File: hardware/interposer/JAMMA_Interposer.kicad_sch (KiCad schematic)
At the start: 5 parts

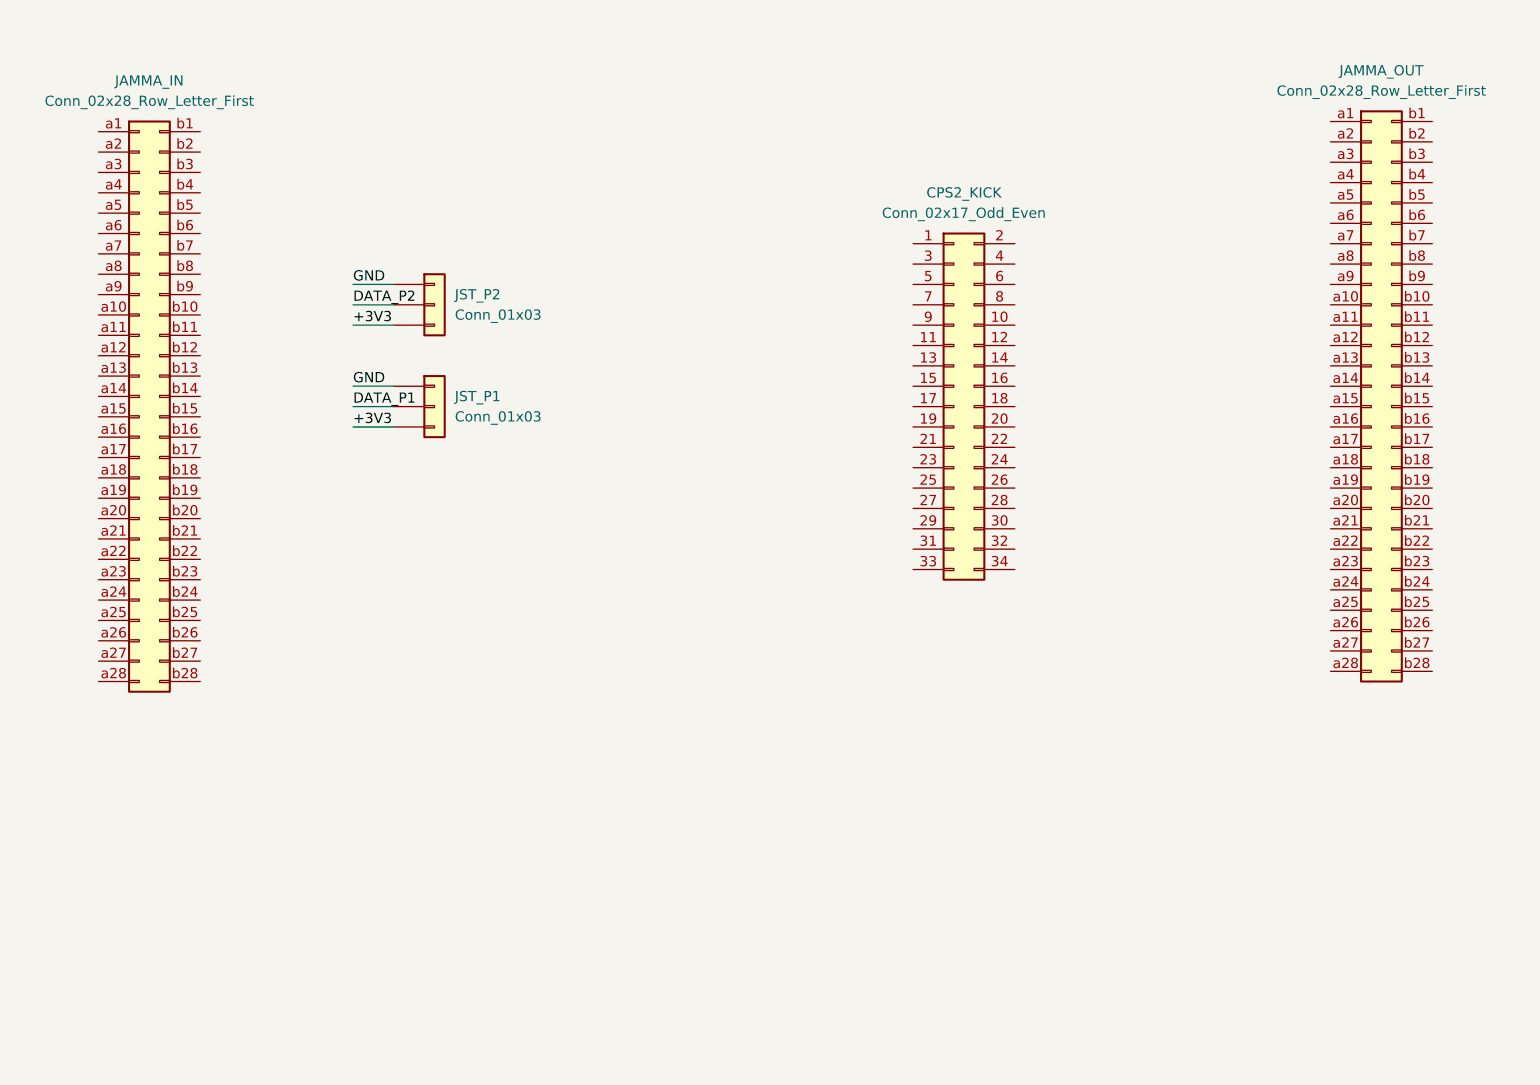
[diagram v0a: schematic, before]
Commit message: Update pin mapping/web assets and interposer schematic baseline
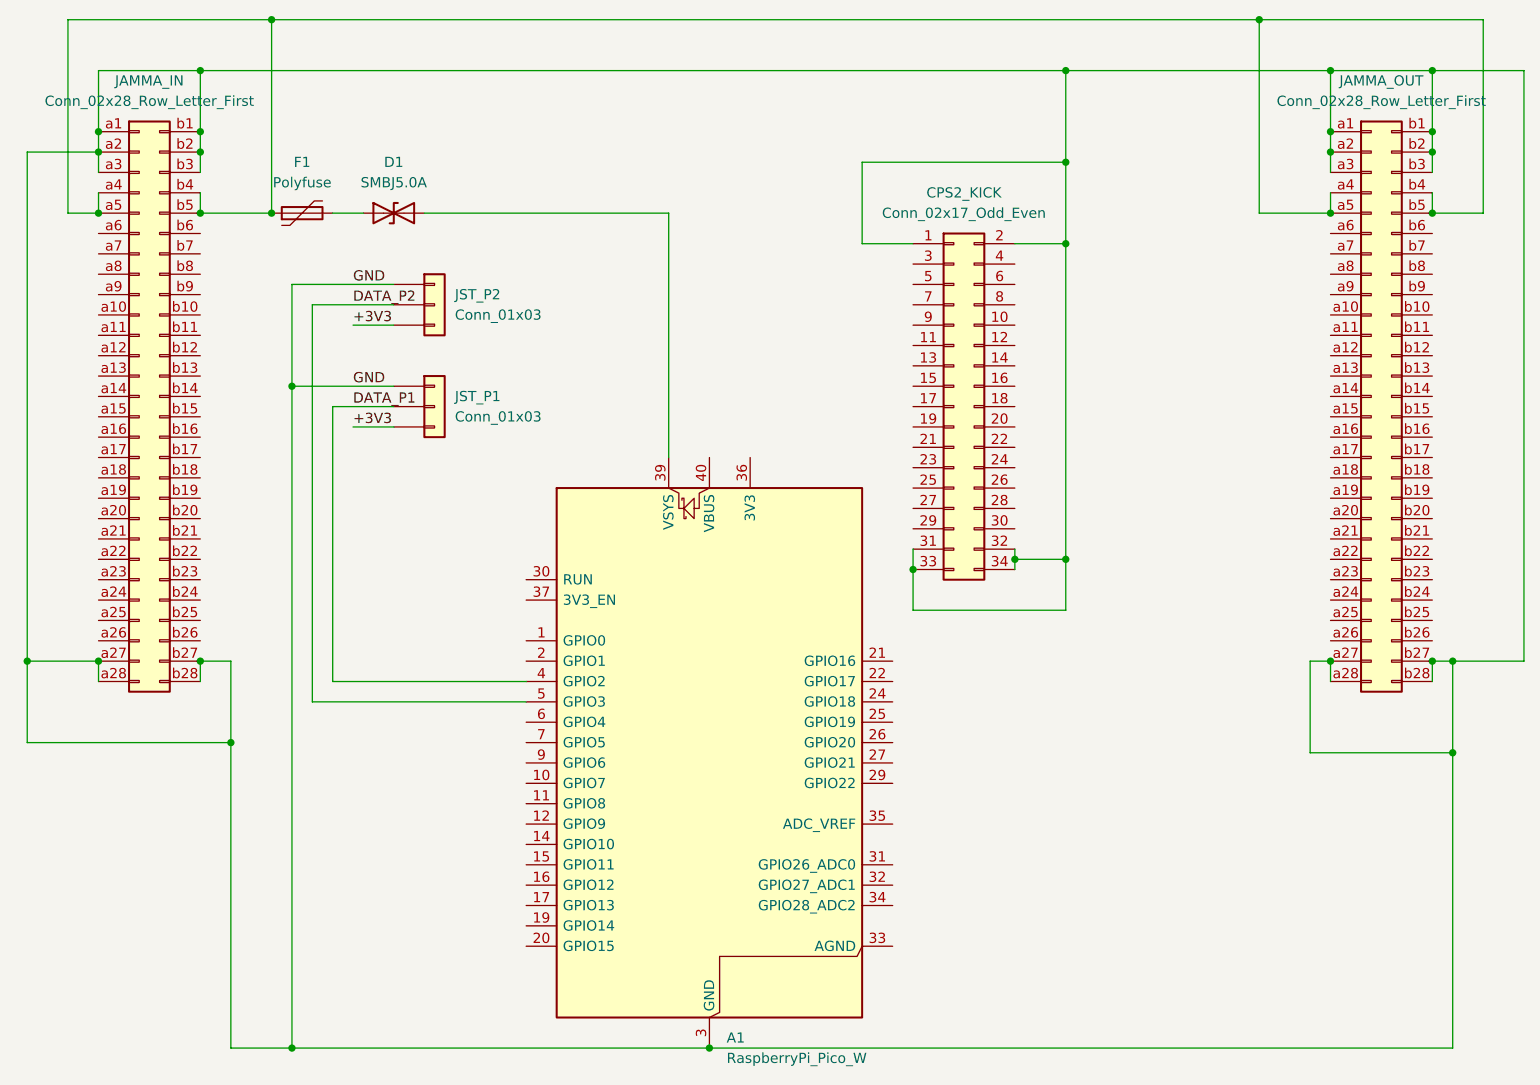
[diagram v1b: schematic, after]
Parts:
- added A1: RaspberryPi_Pico_W, Module:RaspberryPi_Pico_Common_THT, symbol MCU_Module:RaspberryPi_Pico_W
- added D1: SMBJ5.0A, symbol Device:D_TVS
- added F1: Polyfuse, symbol Device:Polyfuse
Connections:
- net DATA_P1: now also A1.4 (GPIO2)
- net DATA_P2: now also A1.5 (GPIO3)
- net GND: now also CPS2_KICK.1 (Pin_1), CPS2_KICK.2 (Pin_2), CPS2_KICK.31 (Pin_31), CPS2_KICK.32 (Pin_32), CPS2_KICK.33 (Pin_33), CPS2_KICK.34 (Pin_34), JAMMA_IN.a1 (Pin_a1), JAMMA_IN.a2 (Pin_a2), JAMMA_IN.a27 (Pin_a27), JAMMA_IN.a28 (Pin_a28), JAMMA_IN.a3 (Pin_a3), JAMMA_IN.b1 (Pin_b1), JAMMA_IN.b2 (Pin_b2), JAMMA_IN.b27 (Pin_b27), JAMMA_IN.b28 (Pin_b28), JAMMA_IN.b3 (Pin_b3), JAMMA_OUT.a1 (Pin_a1), JAMMA_OUT.a2 (Pin_a2), JAMMA_OUT.a27 (Pin_a27), JAMMA_OUT.a28 (Pin_a28), JAMMA_OUT.a3 (Pin_a3), JAMMA_OUT.b1 (Pin_b1), JAMMA_OUT.b2 (Pin_b2), JAMMA_OUT.b27 (Pin_b27), JAMMA_OUT.b28 (Pin_b28), JAMMA_OUT.b3 (Pin_b3), A1.13 (GND), A1.18 (GND), A1.23 (GND), A1.28 (GND), A1.3 (GND), A1.38 (GND), A1.8 (GND)
- net at JAMMA_IN.a4 (Pin_a4): now also JAMMA_IN.a5 (Pin_a5), JAMMA_IN.b4 (Pin_b4), JAMMA_IN.b5 (Pin_b5), JAMMA_OUT.a4 (Pin_a4), JAMMA_OUT.a5 (Pin_a5), JAMMA_OUT.b4 (Pin_b4), JAMMA_OUT.b5 (Pin_b5), F1.1
- new net: D1.1 (A1), F1.2
- new net: A1.39 (VSYS), D1.2 (A2)
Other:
- moved on the sheet: JAMMA_OUT
